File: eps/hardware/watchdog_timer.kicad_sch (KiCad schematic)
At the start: 2 parts, among them U5 TPS35-Q1

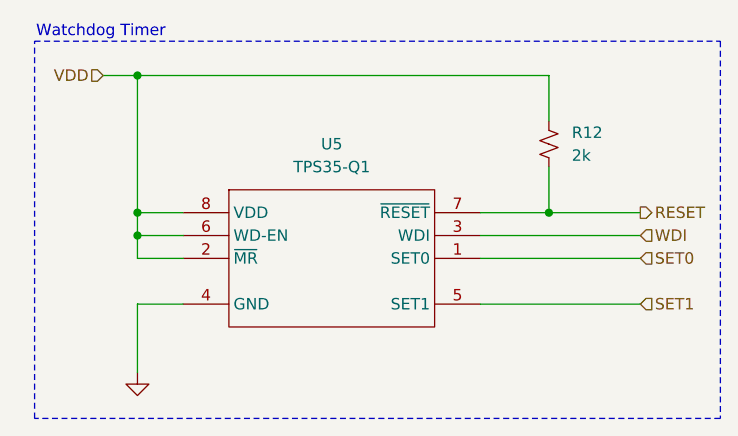
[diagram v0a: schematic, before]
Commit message: reannotate and finish refactor to LTC4162-L
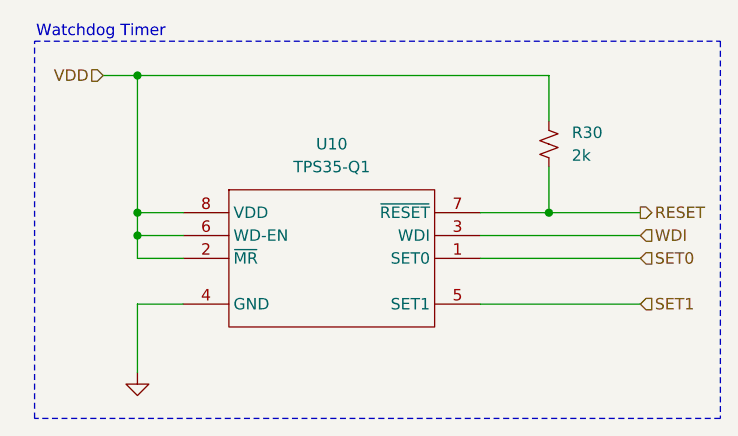
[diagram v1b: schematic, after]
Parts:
- renumbered R12 to R30, U5 to U10
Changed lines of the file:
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@@
 		(dnp no)
 		(fields_autoplaced yes)
-		(property "Reference" "U5"
+		(property "Reference" "U10"
 			(at 46.99 26.67 0)
 			(effects
@@
 			(project ""
 				(path "/9e0ae2e7-d4be-41b4-8312-0d2aceea2180/b94b8a9c-8452-423f-9ecc-cad4cd57e214"
-					(reference "U5")
+					(reference "U10")
 					(unit 1)
 				)
@@
 		(dnp no)
 		(fields_autoplaced yes)
-		(property "Reference" "#PWR030"
+		(property "Reference" "#PWR016"
 			(at 25.4 58.42 0)
 			(effects
@@
 			(project ""
 				(path "/9e0ae2e7-d4be-41b4-8312-0d2aceea2180/b94b8a9c-8452-423f-9ecc-cad4cd57e214"
-					(reference "#PWR030")
+					(reference "#PWR016")
 					(unit 1)
 				)
@@
 		(dnp no)
 		(fields_autoplaced yes)
-		(property "Reference" "R12"
+		(property "Reference" "R30"
 			(at 73.66 25.3999 0)
 			(effects
@@
 			(project ""
 				(path "/9e0ae2e7-d4be-41b4-8312-0d2aceea2180/b94b8a9c-8452-423f-9ecc-cad4cd57e214"
-					(reference "R12")
+					(reference "R30")
 					(unit 1)
 				)

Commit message: add stm32 bsp and reconfigure pinout
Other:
- company: (none) -> SCRT
- title: (none) -> OSUSat CubeSat EPS
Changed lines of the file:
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@@
 	(generator_version "9.0")
 	(paper "A4")
+	(title_block
+		(title "OSUSat CubeSat EPS")
+		(date "2025-08-22")
+		(rev "1")
+		(company "SCRT")
+	)
 	(rectangle
 		(start 13.97 15.24)

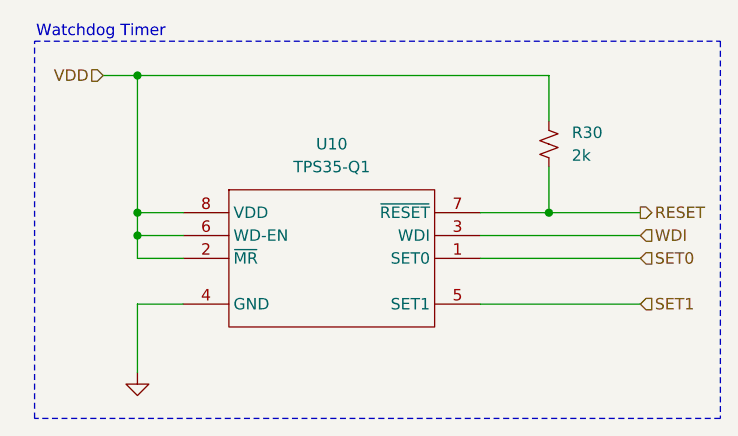
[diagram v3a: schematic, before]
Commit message: fix ERC issues
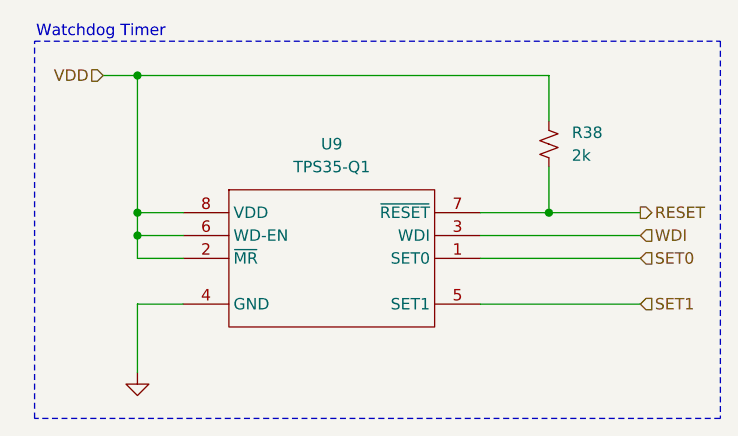
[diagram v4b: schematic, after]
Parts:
- renumbered R30 to R38, U10 to U9
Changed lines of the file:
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@@
 		(dnp no)
 		(fields_autoplaced yes)
-		(property "Reference" "U10"
+		(property "Reference" "U9"
 			(at 46.99 26.67 0)
 			(effects
@@
 			(project ""
 				(path "/9e0ae2e7-d4be-41b4-8312-0d2aceea2180/b94b8a9c-8452-423f-9ecc-cad4cd57e214"
-					(reference "U10")
+					(reference "U9")
 					(unit 1)
 				)
@@
 		(dnp no)
 		(fields_autoplaced yes)
-		(property "Reference" "#PWR016"
+		(property "Reference" "#PWR026"
 			(at 25.4 58.42 0)
 			(effects
@@
 			(project ""
 				(path "/9e0ae2e7-d4be-41b4-8312-0d2aceea2180/b94b8a9c-8452-423f-9ecc-cad4cd57e214"
-					(reference "#PWR016")
+					(reference "#PWR026")
 					(unit 1)
 				)
@@
 		(dnp no)
 		(fields_autoplaced yes)
-		(property "Reference" "R30"
+		(property "Reference" "R38"
 			(at 73.66 25.3999 0)
 			(effects
@@
 			(project ""
 				(path "/9e0ae2e7-d4be-41b4-8312-0d2aceea2180/b94b8a9c-8452-423f-9ecc-cad4cd57e214"
-					(reference "R30")
+					(reference "R38")
 					(unit 1)
 				)

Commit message: fix all ERC errors
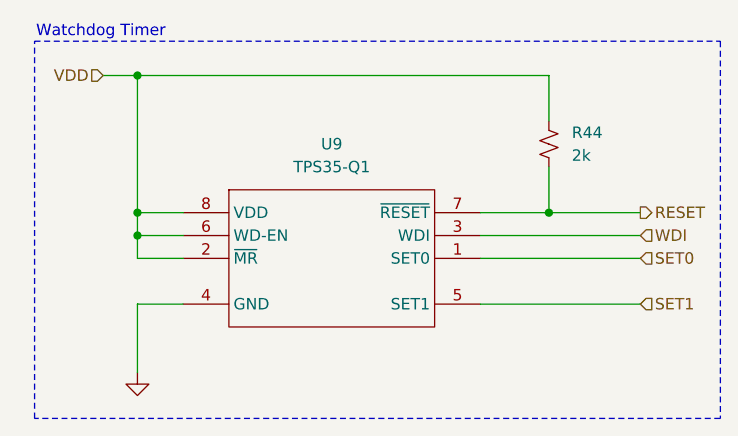
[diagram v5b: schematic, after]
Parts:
- renumbered R38 to R44
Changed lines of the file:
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@@
 		(dnp no)
 		(fields_autoplaced yes)
-		(property "Reference" "#PWR026"
+		(property "Reference" "#PWR028"
 			(at 25.4 58.42 0)
 			(effects
@@
 			(project ""
 				(path "/9e0ae2e7-d4be-41b4-8312-0d2aceea2180/b94b8a9c-8452-423f-9ecc-cad4cd57e214"
-					(reference "#PWR026")
+					(reference "#PWR028")
 					(unit 1)
 				)
@@
 		(dnp no)
 		(fields_autoplaced yes)
-		(property "Reference" "R38"
+		(property "Reference" "R44"
 			(at 73.66 25.3999 0)
 			(effects
@@
 			(project ""
 				(path "/9e0ae2e7-d4be-41b4-8312-0d2aceea2180/b94b8a9c-8452-423f-9ecc-cad4cd57e214"
-					(reference "R38")
+					(reference "R44")
 					(unit 1)
 				)

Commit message: fix all but one warning
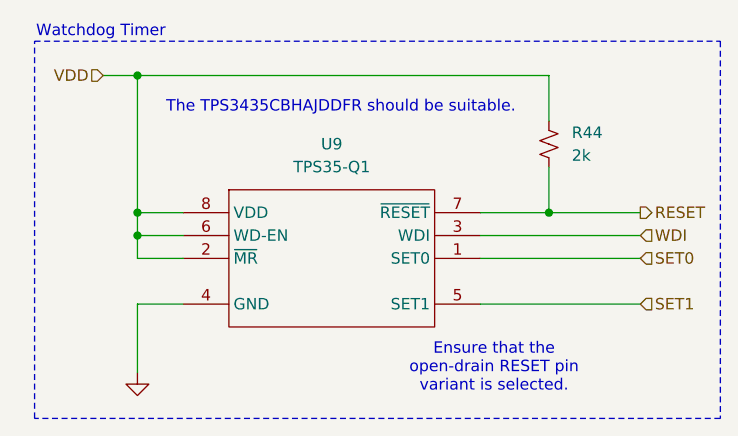
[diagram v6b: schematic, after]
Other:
- note added: "Ensure that the open-drain RESET pin variant is selected."
- note added: "The TPS3435CBHAJDDFR should be suitable."
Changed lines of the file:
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@@
+		)
+	)
+	(text "The TPS3435CBHAJDDFR should be suitable."
+		(exclude_from_sim no)
+		(at 48.006 22.606 0)
+		(effects
+			(font
+				(size 1.27 1.27)
+			)
+		)
+	)
+	(text "Ensure that the\nopen-drain RESET pin\nvariant is selected."
+		(exclude_from_sim no)
+		(at 65.024 51.562 0)
+		(effects
+			(font
+				(size 1.27 1.27)
+			)
 		)
 	)

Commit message: netlist fixes
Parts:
- renumbered R44 to R32
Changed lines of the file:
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@@
 		(dnp no)
 		(fields_autoplaced yes)
-		(property "Reference" "R44"
+		(property "Reference" "R32"
 			(at 73.66 25.3999 0)
 			(effects
@@
 			(project ""
 				(path "/9e0ae2e7-d4be-41b4-8312-0d2aceea2180/b94b8a9c-8452-423f-9ecc-cad4cd57e214"
-					(reference "R44")
+					(reference "R32")
 					(unit 1)
 				)

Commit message: finish footprint assignment and board setup
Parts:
- R32: footprint (none) -> Resistor_SMD:R_0603_1608Metric
- U9: footprint (none) -> Package_TO_SOT_SMD:SOT-23-8
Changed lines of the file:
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@@
 			)
 		)
-		(property "Footprint" ""
+		(property "Footprint" "Package_TO_SOT_SMD:SOT-23-8"
 			(at 46.99 31.75 0)
 			(effects
@@
 			)
 		)
-		(property "Footprint" ""
+		(property "Footprint" "Resistor_SMD:R_0603_1608Metric"
 			(at 71.12 26.67 0)
 			(effects
